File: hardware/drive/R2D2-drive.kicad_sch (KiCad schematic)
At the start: 53 parts, among them J1 1751248, J2 1751248, J3 1751248, J4 1935776, J5 1935776, J6 Conn_01x05_Pin, SW1 PTS636 SM50J SMTR LFS, U1 LM1117MP-3.3, U2 STM32F042F6Px, U3 SN65HVD230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

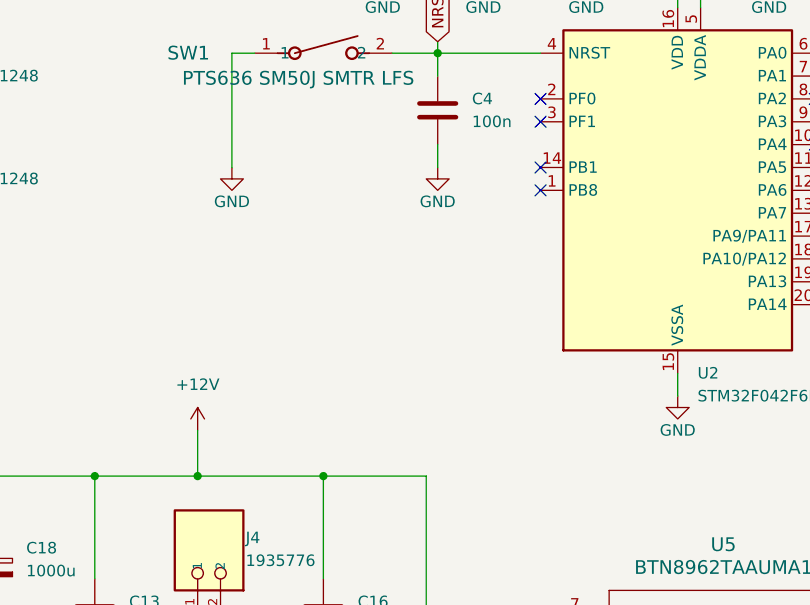
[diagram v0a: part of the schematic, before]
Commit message: hw: drive: added a solder jumper for CAN address
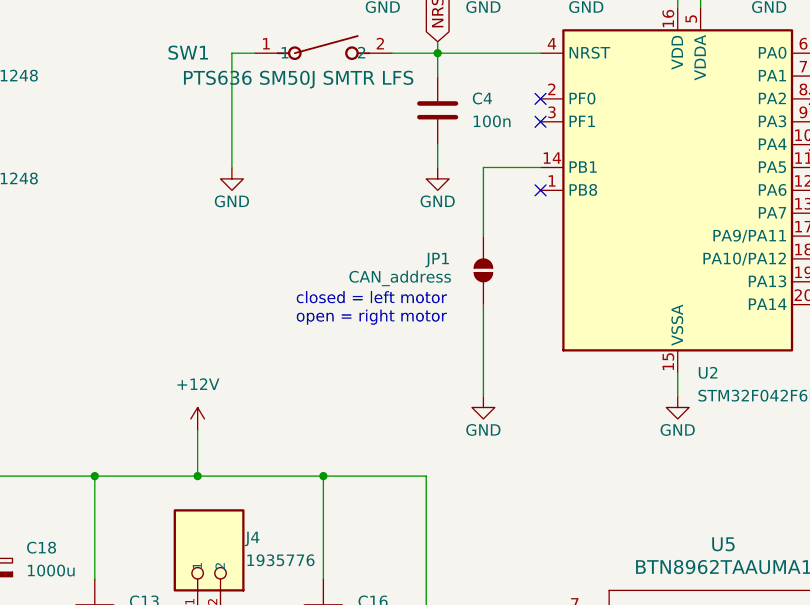
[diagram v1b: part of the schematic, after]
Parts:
- added JP1: CAN_address, Jumper:SolderJumper-2_P1.3mm_Open_TrianglePad1.0x1.5mm, symbol Jumper:SolderJumper_2_Open
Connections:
- net GND: now also JP1.1 (A)
- net at U2.14 (PB1): now also JP1.2 (B)
- no-connect marks 7 -> 6
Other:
- note added: "closed = left motor open = right motor"
- company: (none) -> DAJAKOV
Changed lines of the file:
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@@
 (kicad_sch
-	(version 20231120)
+	(version 20250114)
 	(generator "eeschema")
-	(generator_version "8.0")
+	(generator_version "9.0")
 	(paper "A4")
+	(title_block
+		(date "2025-03-05")
+		(rev "V1.1")
+		(company "DAJAKOV")
+	)
+	(text "closed = left motor\nopen = right motor"
+		(exclude_from_sim no)
+		(at 165.354 75.438 0)
+		(effects
+			(font
+				(size 1.27 1.27)
+			)
+		)
+	)
 	(junction
 		(at 66.04 119.38)
@@
 	)
 	(no_connect
-		(at 184.15 59.69)
-	)
-	(no_connect
 		(at 214.63 52.07)
 	)
@@
 	(wire
 		(pts
+			(xy 177.8 59.69) (xy 184.15 59.69)
+		)
+		(stroke
+			(width 0)
+			(type default)
+		)
+	)
+	(wire
+		(pts
 			(xy 228.6 99.06) (xy 228.6 101.6)
 		)
@@
 	(wire
 		(pts
+			(xy 177.8 67.31) (xy 177.8 59.69)
+		)
+		(stroke
+			(width 0)
+			(type default)
+		)
+	)
+	(wire
+		(pts
 			(xy 224.79 111.76) (xy 228.6 111.76)
 		)
@@
 	(wire
 		(pts
+			(xy 177.8 85.09) (xy 177.8 74.93)
+		)
+		(stroke
+			(width 0)
+			(type default)
+		)
+	)
+	(wire
+		(pts
 			(xy 72.39 57.15) (xy 72.39 63.5)
 		)
@@
 	)
 	(symbol
+		(lib_id "Jumper:SolderJumper_2_Open")
+		(at 177.8 71.12 90)
+		(unit 1)
+		(exclude_from_sim yes)
+		(in_bom no)
+		(on_board yes)
+		(dnp no)
+		(property "Reference" "JP1"
+			(at 171.45 69.85 90)
+			(effects
+				(font
+					(size 1.27 1.27)
+				)
+				(justify right)
+			)
+		)
+		(property "Value" "CAN_address"
+			(at 162.814 71.882 90)
+			(effects
+				(font
+					(size 1.27 1.27)
+				)
+				(justify right)
+			)
+		)
+		(property "Footprint" "Jumper:SolderJumper-2_P1.3mm_Open_TrianglePad1.0x1.5mm"
+			(at 177.8 71.12 0)
+			(effects
+				(font
+					(size 1.27 1.27)
+				)
+				(hide yes)
+			)
+		)
+		(property "Datasheet" "~"
+			(at 177.8 71.12 0)
+			(effects
+				(font
+					(size 1.27 1.27)
+				)
+				(hide yes)
+			)
+		)
+		(property "Description" "Solder Jumper, 2-pole, open"
+			(at 177.8 71.12 0)
+			(effects
+				(font
+					(size 1.27 1.27)
+				)
+				(hide yes)
+			)
+		)
+		(pin "2"
+		)
+		(pin "1"
+		)
+		(instances
+			(project ""
+				(path "/8db0bf65-be4b-40cc-a536-d7c303f1663e"
+					(reference "JP1")
+					(unit 1)
+				)
+			)
+		)
+	)
+	(symbol
 		(lib_id "Connector:TestPoint")
 		(at 269.24 43.18 0)
@@
 	)
 	(symbol
+		(lib_id "power:GND")
+		(at 177.8 85.09 0)
+		(unit 1)
+		(exclude_from_sim no)
+		(in_bom yes)
+		(on_board yes)
+		(dnp no)
+		(property "Reference" "#PWR033"
+			(at 177.8 91.44 0)
+			(effects
+				(font
+					(size 1.27 1.27)
+				)
+				(hide yes)
+			)
+		)
+		(property "Value" "GND"
+			(at 177.8 88.9 0)
+			(effects
+				(font
+					(size 1.27 1.27)
+				)
+			)
+		)
+		(property "Footprint" ""
+			(at 177.8 85.09 0)
+			(effects
+				(font
+					(size 1.27 1.27)
+				)
+				(hide yes)
+			)
+		)
+		(property "Datasheet" ""
+			(at 177.8 85.09 0)
+			(effects
+				(font
+					(size 1.27 1.27)
+				)
+				(hide yes)
+			)
+		)
+		(property "Description" "Power symbol creates a global label with name \"GND\" , ground"
+			(at 177.8 85.09 0)
+			(effects
+				(font
+					(size 1.27 1.27)
+				)
+				(hide yes)
+			)
+		)
+		(pin "1"
+		)
+		(instances
+			(project "R2D2-drive"
+				(path "/8db0bf65-be4b-40cc-a536-d7c303f1663e"
+					(reference "#PWR033")
+					(unit 1)
+				)
+			)
+		)
+	)
+	(symbol
 		(lib_name "BTN8962TAAUMA1_2")
 		(lib_id "BTN8962TAAUMA1:BTN8962TAAUMA1")
@@
 		)
 	)
+	(embedded_fonts no)
 )
